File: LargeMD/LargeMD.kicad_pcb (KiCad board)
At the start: 2 copper layers, 110 x 60 mm, 189 parts, among them J1 Conn_01x02_Male, J10 Conn_01x04_Male, J2 Conn_01x02_Female, J3 Conn_01x10_Male, J4 Conn_01x02_Male, J5 Conn_01x03_Male, J6 Conn_01x02_Female, J7 Conn_01x04_Male, J8 Conn_01x04_Male, J9 Conn_01x04_Male, Q1 TJ60S04M3L, Q10 S8050, Q11 SSM3J332R, Q12 S8050, Q13 SSM3J332R, Q14 S8050, Q15 S8050, Q16 S8050, Q17 BSS138, Q18 BSS138, Q19 TPH3R704PL, Q2 BSS138, Q20 TPH3R704PL, Q21 TPH3R704PL, Q22 TPH3R704PL, Q3 TJ60S04M3L, Q4 S8050, Q5 SSM3J332R, Q6 S8050, Q7 SSM3J332R, Q8 S8050, Q9 SSM3J332R, SW1 SW_DIP_x05, SW2 SW_SPDT, SW3 SW_SPDT, SW4 SW_SPST, U1 LF50_TO220, U10 IR2302, U2 AZ1084CD-3.3, U3 STM32C031K4T6, U4 LT6106, U5 MAX3485, U6 MAX3485, U7 TLP2361, U8 TLP2361, U9 IR2302, Y1 48MHz

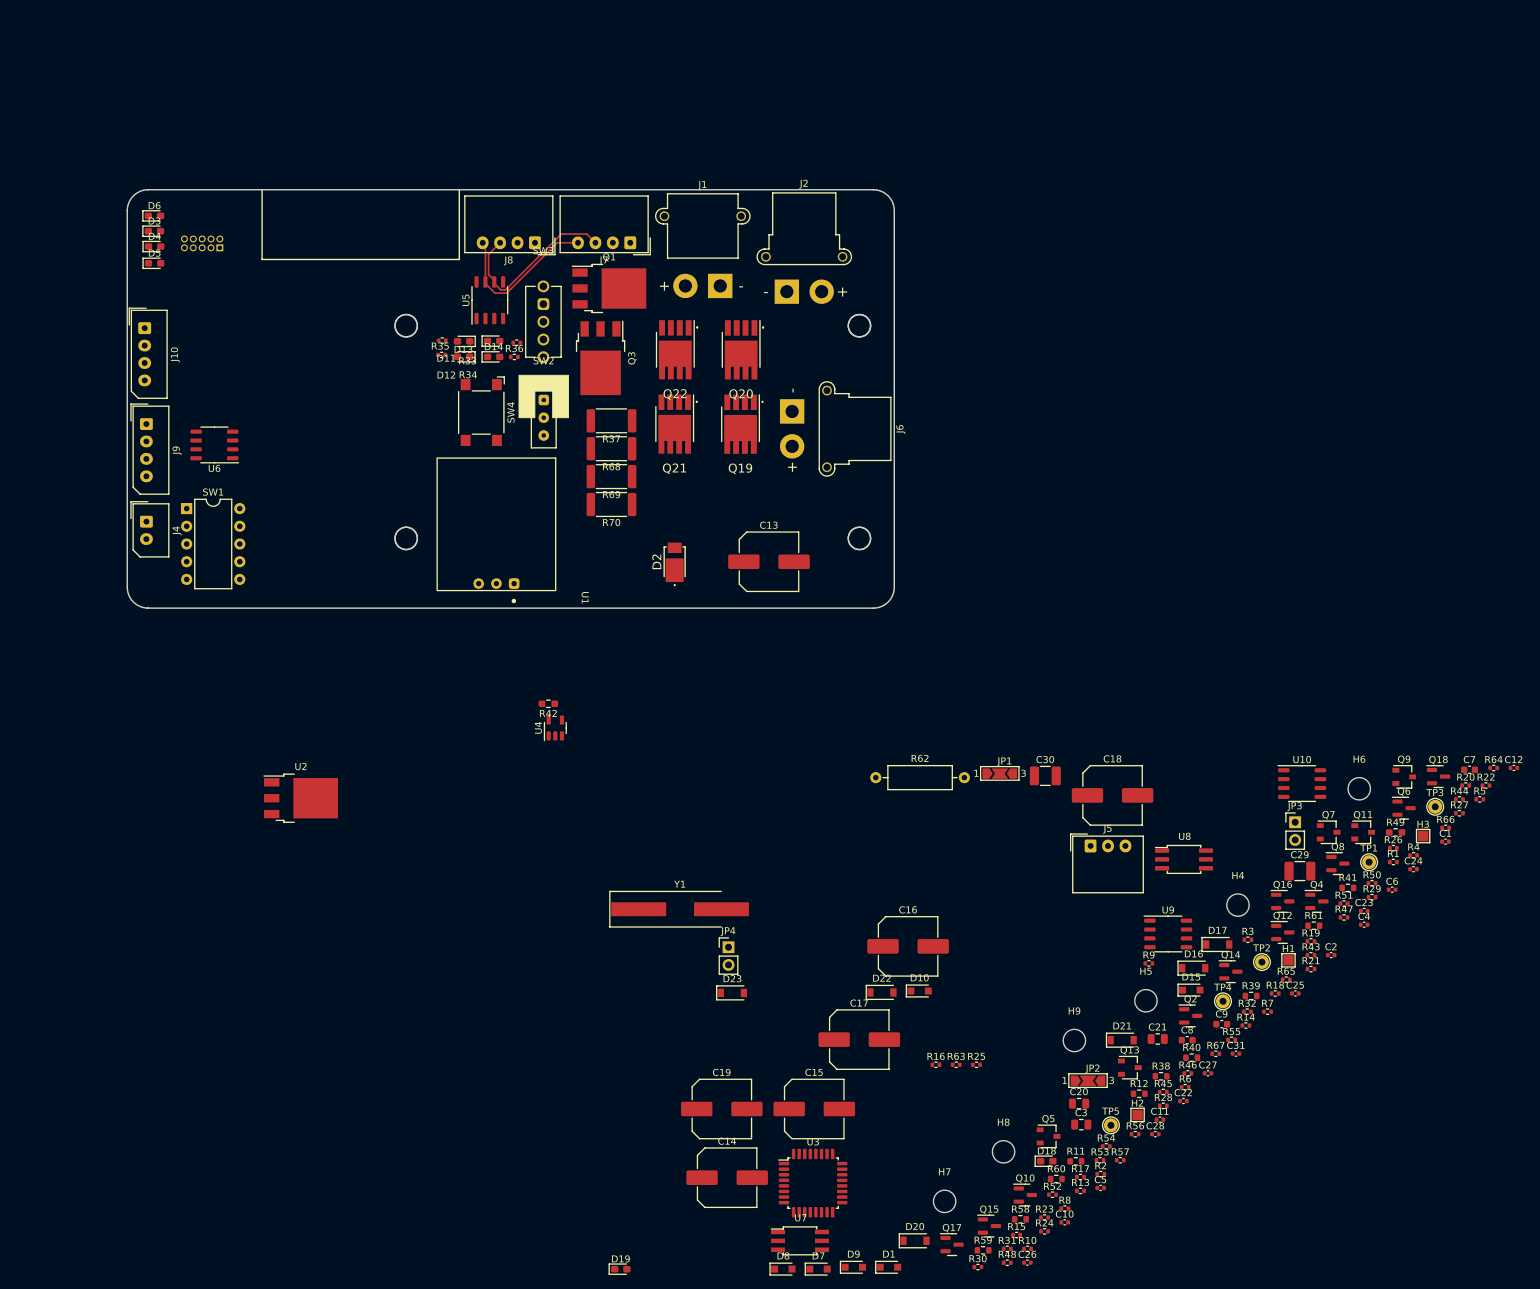
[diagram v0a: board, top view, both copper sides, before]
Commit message: エンコーダー基板配線完了
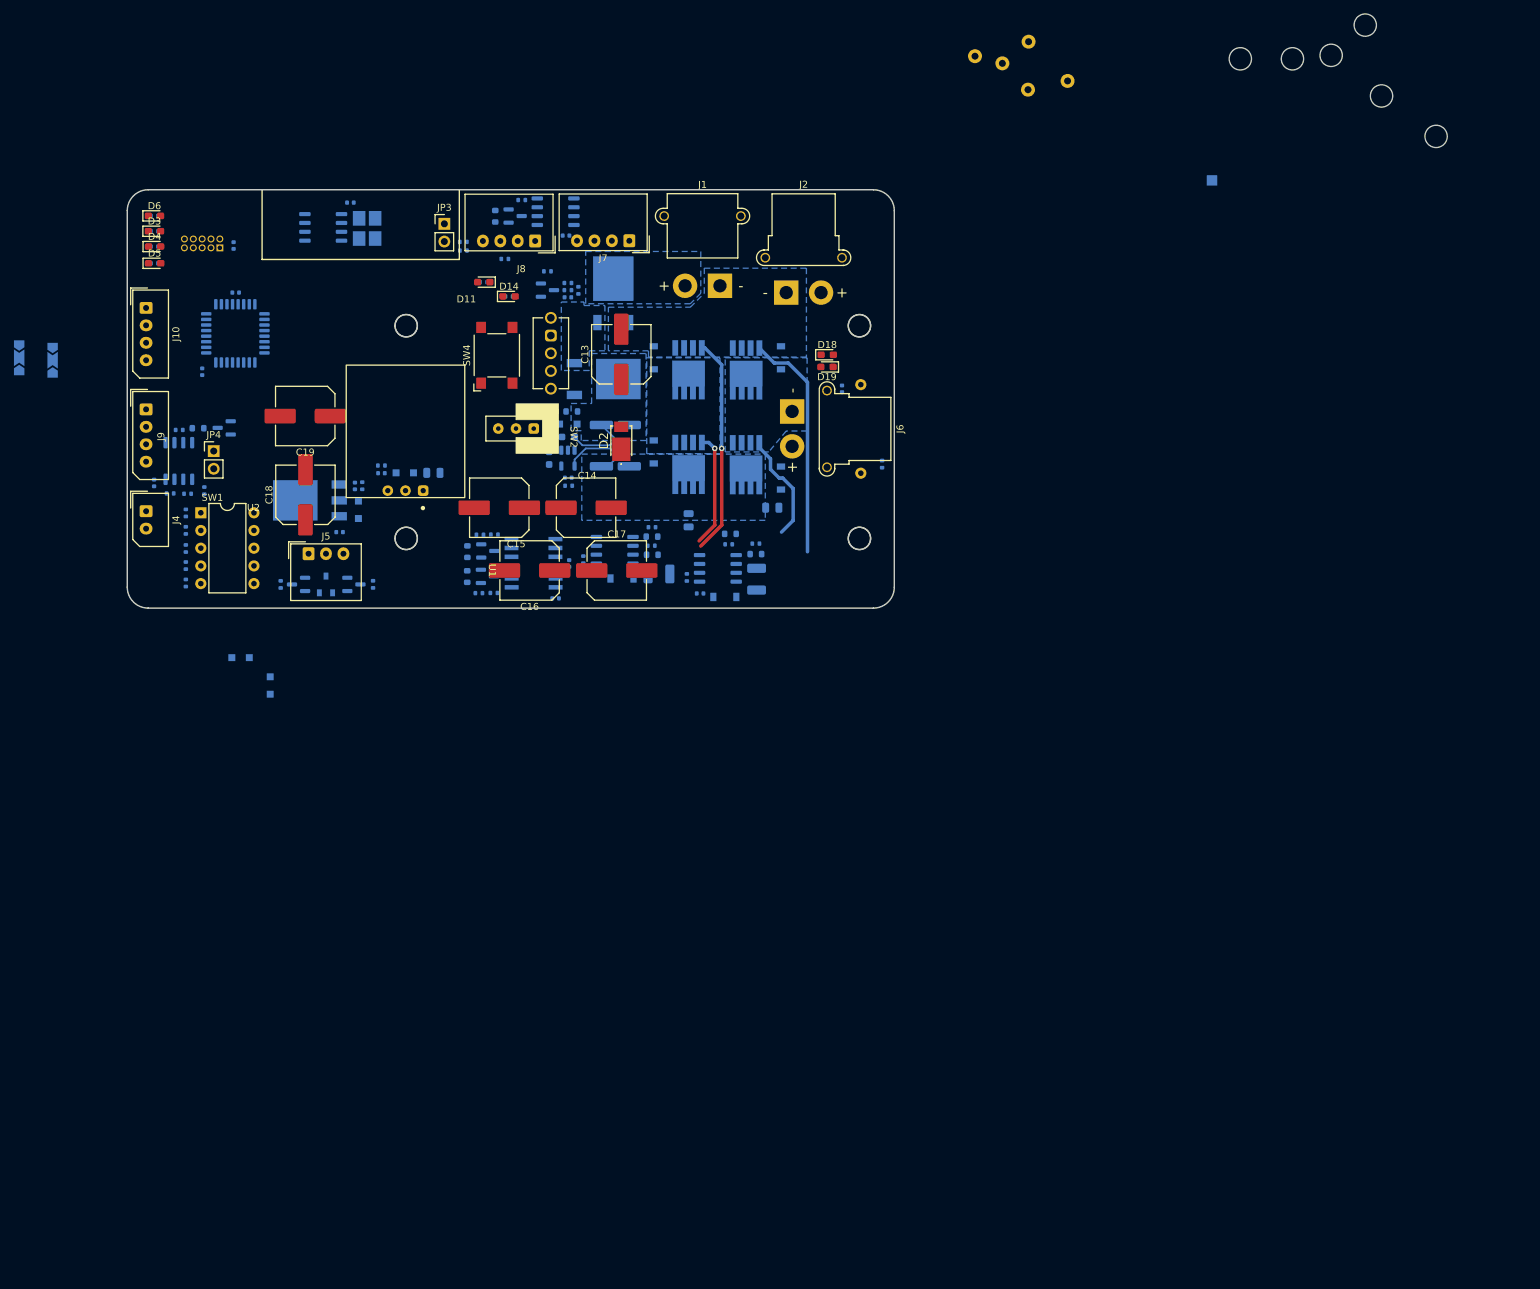
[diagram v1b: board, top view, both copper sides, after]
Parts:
- removed C12: 1uF, Capacitor_SMD:C_0402_1005Metric
- removed C8, C9: 22pF, Capacitor_SMD:C_0603_1608Metric
- removed D10: D_Zener, Diode_SMD:D_SOD-323_HandSoldering
- removed D12, D13: Green, LED_SMD:LED_0603_1608Metric_Pad1.05x0.95mm_HandSolder
- removed H1, H3: MountingHole_Pad, TestPoint:TestPoint_Pad_1.5x1.5mm
- removed Q10, Q12, Q14, Q8: S8050, Package_TO_SOT_SMD:SOT-23
- removed Q11, Q13, Q7, Q9: SSM3J332R, Package_TO_SOT_SMD:SOT-23W
- removed R21, R23, R25, R26, R28, R29, R30, R31, R32: 10k, Resistor_SMD:R_0402_1005Metric
- removed R24, R34, R35: 1k, Resistor_SMD:R_0402_1005Metric
- removed R27: 100k, Resistor_SMD:R_0402_1005Metric
- removed R69, R70: 40mR, Resistor_SMD:R_2512_6332Metric
- added U11: NJU6319AE, Package_SO:SOP-8_3.9x4.9mm_P1.27mm, B.Cu at (70.6, 40.5)
- C1, C10, C11, C2, C20, C21, C22, C23, C24, C25, C26, C27, C28, C29, C3, C30, C31, C4, C5, C6, D1, D15, D16, D17, D20, D21, D22, D23, D7, D8, D9, H2, H4, H5, H6, H7, H8, H9, JP1, JP2, Q15, Q16, Q17, Q18, Q19, Q2, Q20, Q21, Q22, Q4, Q5, Q6, R1, R10, R11, R12, R13, R14, R15, R16, R17, R18, R19, R2, R20, R22, R3, R33, R36, R38, R39, R4, R40, R41, R42, R43, R44, R45, R46, R47, R48, R49, R5, R50, R51, R52, R53, R54, R55, R56, R57, R58, R59, R6, R60, R61, R62, R63, R64, R65, R66, R67, R7, R8, R9, TP1, TP2, TP3, TP4, TP5, U10, U2, U3, U4, U5, U6, U7, U8, U9: moved to B.Cu
- C7: value ADJ_ST -> 0.1uF; footprint Capacitor_SMD:C_0603_1608Metric -> Capacitor_SMD:C_0402_1005Metric; moved to B.Cu
- Q1, Q3: footprint Package_TO_SOT_SMD:TO-252-3_TabPin2 -> Package_TO_SOT_SMD:TO-252-2; moved to B.Cu
- R37, R68: value 40mR -> 20mR; moved to B.Cu
- Y1: value 48MHz -> 16MHz; footprint Crystal:Crystal_SMD_HC49-SD_HandSoldering -> Crystal:Crystal_SMD_3225-4Pin_3.2x2.5mm_HandSoldering; moved to B.Cu
- moved R14 192.3 mm to (46.4, 43.3), turned to 180 degrees
- moved R13 191.3 mm to (46.4, 41.1), turned to 180 degrees
- moved R5 188.6 mm to (50.9, 89.0), turned to 90 degrees
- moved C2 187.4 mm to (57.8, 43.1), turned to 90 degrees
- moved R15 186.3 mm to (46.4, 45.7), turned to 180 degrees
- moved JP2 185.1 mm to (27.0, 59.2), turned to -90 degrees
- moved R1 180.3 mm to (50.9, 81.5), turned to 90 degrees
- moved C7 179.9 mm to (74.5, 37.0)
- moved C11 177.9 mm to (58.0, 49.9)
- moved R41 177.6 mm to (52.6, 69.3), turned to 180 degrees
- moved C10 173.7 mm to (53.2, 61.2), turned to -90 degrees
- moved R46 171.6 mm to (50.0, 69.6)
- moved H7 170.5 mm to (222.4, 21.7), turned to 180 degrees
- moved C26 167.9 mm to (46.4, 77.2), turned to -90 degrees
- moved R22 166.8 mm to (76.2, 77.6), turned to -90 degrees
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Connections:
- C31 pad 2: Motor_B -> Motor_A
- C6 pad 1: /3.3VSYS -> +3.3V
- C7 pad 1: GND -> +3.3V
- C7 pad 2: Net-(C7-Pad2) -> GND
- D18 pad 1: Motor_B -> Motor_A
- D19 pad 2: Motor_B -> Motor_A
- D8 pad 2: /3.3VSYS -> +3.3V
- R22 pad 2: /3.3VSYS -> +3.3V
- R62 pad 1: Motor_A -> Motor_B
- R67 pad 2: Motor_A -> Motor_B
- U2 pad 2: /3.3VSYS -> +3.3V
- U3 pad 2: unconnected-(U3-Pad2) -> OSC_IN
- U3 pad 6: unconnected-(U3-Pad6) -> NRST
- Y1 pad 1: OSC_OUT -> Net-(U11-Pad2)
- Y1 pad 2: OSC_IN -> GND
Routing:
- net Net-(Q20-Pad4): track 0.00 -> 33.2 mm
- net Net-(Q22-Pad4): track 0.00 -> 31.1 mm, vias 0 -> 1
- net RS485a_A: track 25.6 -> 0.00 mm
- net RS485a_B: track 22.8 -> 0.52 mm
- net Net-(Q21-Pad4): track 0.00 -> 16.4 mm, vias 0 -> 1
- net Net-(Q19-Pad4): track 0.00 -> 15.8 mm
- net Vdrive: track 0.00 -> 10.7 mm
- net VDD: track 0.00 -> 9.46 mm
- added copper zone on B.Cu, net /12VBAT
- added copper zone on B.Cu, net /S-S
- added copper zone on B.Cu, net GND
- added copper zone on B.Cu, net Motor_A
- added copper zone on B.Cu, net Motor_B
- added copper zone on B.Cu, net VDD
- added copper zone on B.Cu, net Vdrive

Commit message: LargeMD
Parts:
- removed C2: 0.1uF, Capacitor_SMD:C_0402_1005Metric
- moved TP1 44.8 mm to (158.8, 60.9)
- moved JP2 28.2 mm to (54.6, 53.5), turned to 90 degrees
- moved JP1 20.7 mm to (51.5, 53.5)
- moved R50 13.1 mm to (108.9, 40.6), turned to 0 degrees
- moved C10 11.3 mm to (64.3, 58.7)
- moved U3 11.3 mm to (69.0, 53.2)
- moved C11 11.3 mm to (69.0, 47.4)
- moved R9 11.0 mm to (97.6, 56.0), turned to 90 degrees
- moved D2 10.8 mm to (102.7, 72.8), turned to 0 degrees
- moved C1 8.88 mm to (98.6, 56.0), turned to -90 degrees
- moved R8 8.80 mm to (99.7, 56.0), turned to -90 degrees
- moved R7 7.68 mm to (100.9, 54.0)
- moved R4 7.52 mm to (99.4, 62.5), turned to 180 degrees
- moved R10 5.49 mm to (100.9, 52.0), turned to -90 degrees
- moved Q2 5.43 mm to (98.6, 53.0), turned to -90 degrees
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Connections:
- J3 pad 1: /3.3VBUS -> unconnected-(J3-Pad1)
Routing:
- net +5V: track 0.00 -> 102.2 mm
- net +3.3V: track 0.00 -> 64.7 mm, vias 0 -> 3
- net Motor_A: track 0.00 -> 54.4 mm, vias 0 -> 60
- net Motor_B: track 0.00 -> 47.3 mm, vias 0 -> 113
- net Net-(J4-Pad2): track 0.00 -> 39.9 mm
- net VCC: track 0.00 -> 35.8 mm
- net RS485b_A: track 0.00 -> 32.2 mm
- net RS485a_A: track 0.00 -> 31.1 mm
- net RS485b_B: track 0.00 -> 28.2 mm
- net RS485a_B: track 0.52 -> 26.2 mm
- net Net-(R54-Pad2): track 0.00 -> 24.0 mm
- net SHDN: track 0.00 -> 20.9 mm
- net Net-(D18-Pad2): track 0.00 -> 18.3 mm, vias 0 -> 1
- net Net-(C1-Pad2): track 0.00 -> 13.0 mm
- net STLinkTX: track 0.00 -> 12.9 mm
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- added copper zone on F.Cu, net GND
- added copper zone on F.Cu, net Motor_A
- added copper zone on F.Cu, net Motor_B
- added copper zone on F.Cu, net VCC
- added copper zone on F.Cu, net VDD
- added copper zone on F.Cu, net Vdrive

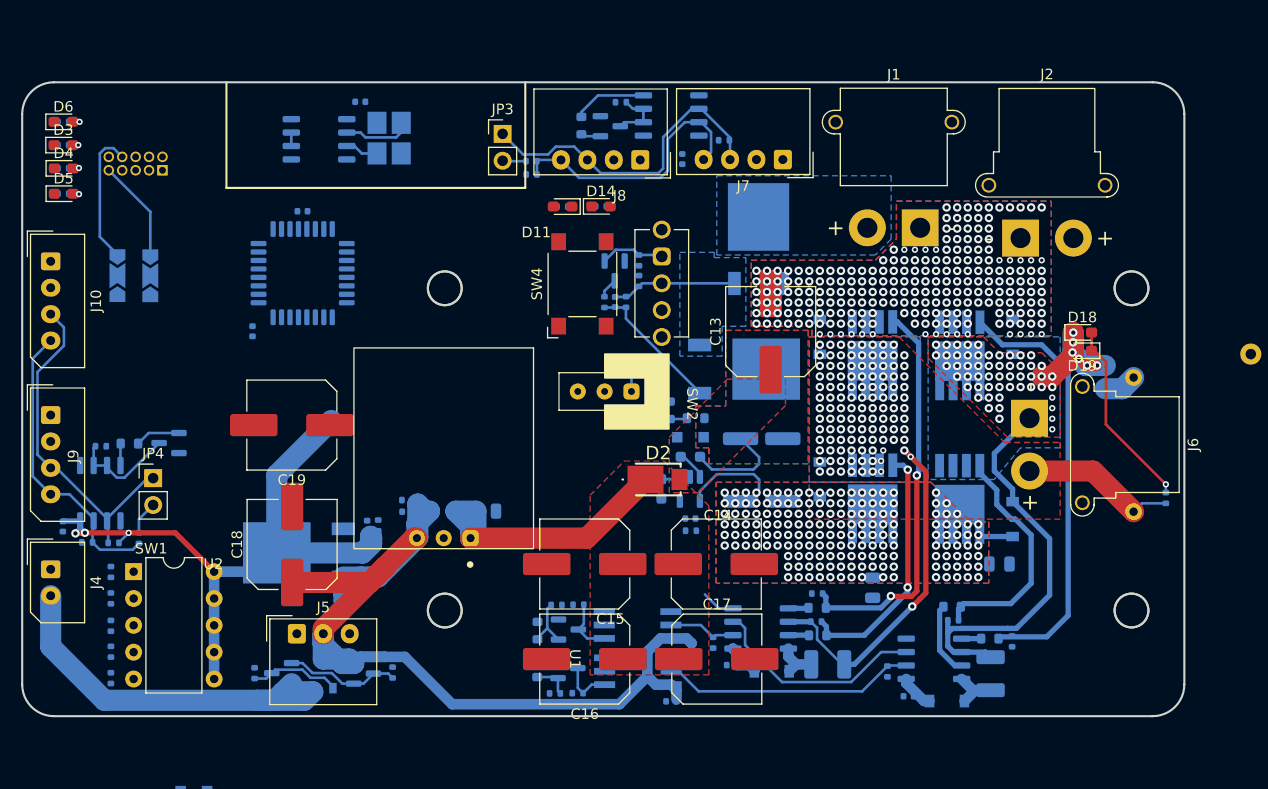
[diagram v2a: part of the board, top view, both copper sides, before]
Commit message: 人力曲面配線中
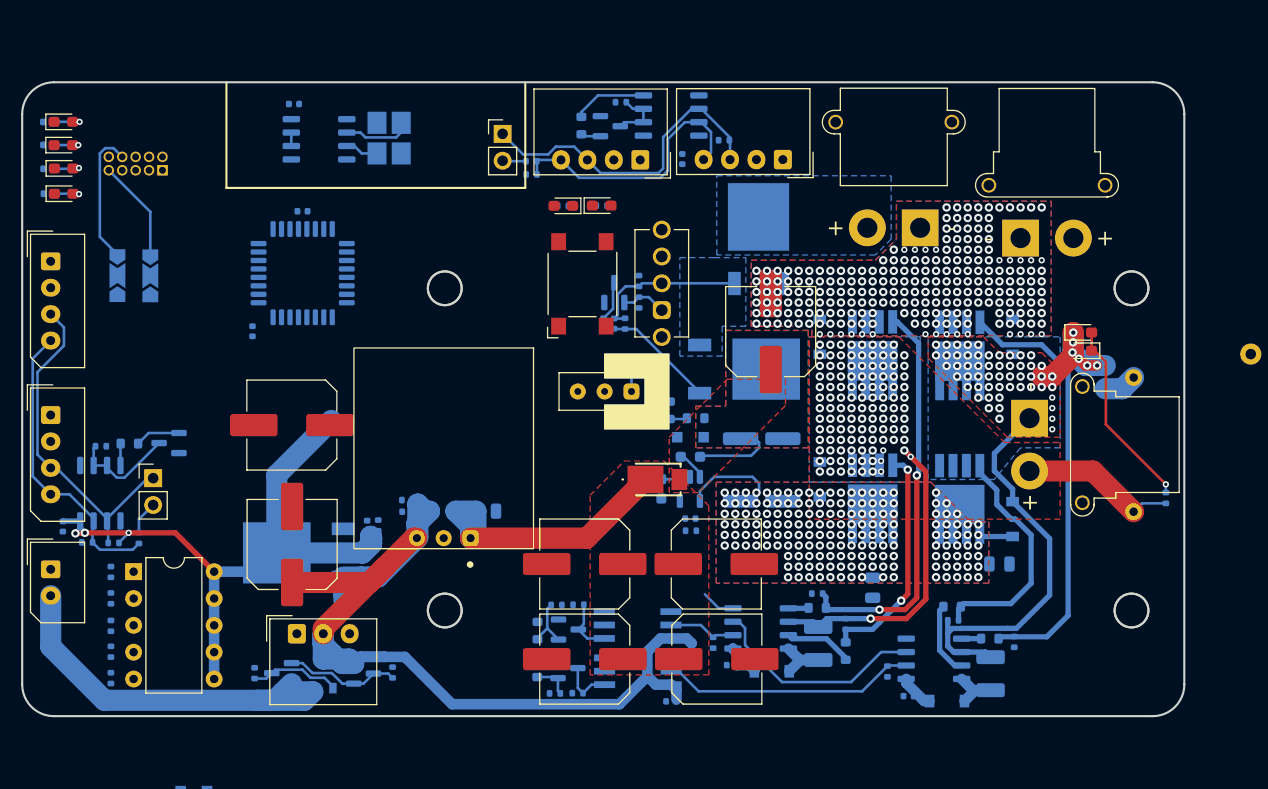
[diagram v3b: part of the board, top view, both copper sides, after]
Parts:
- moved C7 6.27 mm to (68.2, 37.2)
- moved R10 3.99 mm to (100.9, 56.0)
- moved R60 3.04 mm to (120.5, 89.0), turned to 90 degrees
- moved R65 2.80 mm to (120.4, 86.4), turned to -90 degrees
- moved C30 2.17 mm to (117.8, 88.3), turned to 90 degrees
- moved Q2 2.05 mm to (98.5, 55.1), turned to 90 degrees
- moved C1 2.05 mm to (98.5, 58.0)
- moved R8 2.05 mm to (99.6, 58.0)
- moved R9 2.04 mm to (97.5, 58.0)
- moved R16 1.43 mm to (45.0, 38.9)
- moved R13 1.42 mm to (45.0, 41.1)
- moved R14 1.41 mm to (45.0, 43.3)
- moved R15 1.38 mm to (45.0, 45.7)
- moved R64 0.21 mm to (136.4, 88.1)
- moved R33 0.10 mm to (93.7, 46.9)
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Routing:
- net Net-(R60-Pad1): track 1.96 -> 6.49 mm
- net Motor_B: track 47.3 -> 44.1 mm
- net /S-S: track 11.8 -> 15.0 mm
- net Net-(Q21-Pad4): track 24.1 -> 21.9 mm
- net Net-(Q2-Pad3): track 1.90 -> 3.79 mm
- net 主電源スイッチ: track 6.11 -> 4.26 mm
- net Net-(D6-Pad2): track 1.68 -> 3.11 mm
- net Net-(D3-Pad2): track 1.44 -> 2.86 mm
- net Net-(D4-Pad2): track 1.55 -> 2.98 mm
- net Net-(C1-Pad2): track 13.0 -> 11.7 mm
- net Net-(D5-Pad2): track 1.58 -> 2.96 mm
- net VDD: track 9.46 -> 8.34 mm
- net Net-(C30-Pad1): track 4.15 -> 4.75 mm

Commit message: LargeMDほぼ完成
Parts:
- removed H4, H5, H6, H7, H8, H9: MountingHole, MountingHole:MountingHole_3.2mm_M3
- removed TP1, TP2, TP3: TestPoint, TestPoint:TestPoint_THTPad_D2.0mm_Drill1.0mm
- H2: moved to F.Cu
- U3: value STM32C031K4T6 -> STM32G030K6T6
- moved TP4 112.9 mm to (76.6, 70.3)
- moved H2 110.4 mm to (89.1, 51.6), turned to 0 degrees
- moved D15 47.9 mm to (95.7, 71.2), turned to 45 degrees
- moved TP5 45.0 mm to (149.1, 59.8)
- moved D9 32.8 mm to (66.9, 70.5)
- moved C10 9.83 mm to (70.4, 51.0), turned to 45 degrees
- moved U11 5.61 mm to (71.4, 46.1)
- moved Y1 5.61 mm to (78.1, 46.0)
- moved C7 5.61 mm to (69.1, 42.8)
- moved U3 4.21 mm to (65.1, 54.7), turned to -135 degrees
- moved JP2 3.76 mm to (52.6, 56.6), turned to 0 degrees
- moved C19 2.95 mm to (68.3, 70.5), turned to 0 degrees
- moved C11 2.52 mm to (69.3, 49.9), turned to 45 degrees
- moved JP1 1.19 mm to (52.6, 52.9), turned to 0 degrees
- moved C18 1.06 mm to (68.3, 79.9), turned to 180 degrees
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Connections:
- net RS485bRX renamed RS485aRX
- net RS485bTX renamed RS485aTX
- J10 pad 3: RS485b_A -> RS485a_A
- J10 pad 4: RS485b_B -> RS485a_B
- J7 pad 3: RS485a_A -> RS485b_A
- J7 pad 4: RS485a_B -> RS485b_B
- J8 pad 3: RS485a_A -> RS485b_A
- J8 pad 4: RS485a_B -> RS485b_B
- J9 pad 3: RS485b_A -> RS485a_A
- J9 pad 4: RS485b_B -> RS485a_B
- JP1 pad 2: MainRX_RS485bTX -> MainRX1_RS485aTX
- JP2 pad 2: MainTX_RS485bRX -> MainTX1_RS485aRX
- JP3 pad 1: RS485a_A -> RS485b_A
- JP4 pad 1: RS485b_A -> RS485a_A
- R40 pad 2: MainTX_RS485aRX -> MainTX2_RS485bRX
- R50 pad 2: RS485a_A -> RS485b_A
- R51 pad 1: RS485a_B -> RS485b_B
- R52 pad 2: RS485b_A -> RS485a_A
- R53 pad 1: RS485b_B -> RS485a_B
- R56 pad 2: RS485a_B -> RS485b_B
- R57 pad 2: RS485b_B -> RS485a_B
- U11 pad 6: Net-(U11-Pad6) -> unconnected-(U11-Pad6)
- U11 pad 7: Net-(U11-Pad6) -> unconnected-(U11-Pad7)
- U3 pad 10: unconnected-(U3-Pad10) -> V_Measure
- U3 pad 11: unconnected-(U3-Pad11) -> Current_Sence
- U3 pad 12: unconnected-(U3-Pad12) -> SHDN
- U3 pad 13: unconnected-(U3-Pad13) -> PWM_A
- U3 pad 15: unconnected-(U3-Pad15) -> Sensor0
- U3 pad 16: unconnected-(U3-Pad16) -> DIP_SW4
- U3 pad 17: unconnected-(U3-Pad17) -> DIP_SW3
- U3 pad 18: unconnected-(U3-Pad18) -> DIP_SW2
- U3 pad 19: unconnected-(U3-Pad19) -> MainTX1_RS485aRX
- U3 pad 20: unconnected-(U3-Pad20) -> DIP_SW1
- U3 pad 21: unconnected-(U3-Pad21) -> MainRX1_RS485aTX
- U3 pad 22: unconnected-(U3-Pad22) -> DIP_SW0
- U3 pad 24: unconnected-(U3-Pad24) -> TMS
- U3 pad 25: unconnected-(U3-Pad25) -> TCK
- U3 pad 26: unconnected-(U3-Pad26) -> MainRX2_RS485bTX
- U3 pad 27: unconnected-(U3-Pad27) -> LED2
- U3 pad 28: unconnected-(U3-Pad28) -> LED1
- U3 pad 29: unconnected-(U3-Pad29) -> LED0
- U3 pad 30: unconnected-(U3-Pad30) -> PWM_B
- U3 pad 31: unconnected-(U3-Pad31) -> MonitorLED0
- U3 pad 8: unconnected-(U3-Pad8) -> Slide_SW0
- U3 pad 9: unconnected-(U3-Pad9) -> MainTX2_RS485bRX
- U5 pad 1: MainRX_RS485aTX -> MainRX2_RS485bTX
- U5 pad 4: MainTX_RS485aRX -> MainTX2_RS485bRX
- U5 pad 6: RS485a_A -> RS485b_A
- U5 pad 7: RS485a_B -> RS485b_B
- U6 pad 6: RS485b_A -> RS485a_A
- U6 pad 7: RS485b_B -> RS485a_B
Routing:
- net GND: track 3.20 -> 267.0 mm, vias 225 -> 679
- net +3.3V: track 64.7 -> 246.8 mm, vias 3 -> 13
- net NRST: track 0.00 -> 61.8 mm, vias 0 -> 2
- net SHDN: track 20.9 -> 75.1 mm
- net PWM_B: track 0.00 -> 52.5 mm, vias 0 -> 2
- net MainRX2_RS485bTX: track 0.00 -> 50.6 mm
- net PWM_A: track 0.00 -> 46.8 mm
- net MainTX2_RS485bRX: track 0.00 -> 43.8 mm, vias 0 -> 2
- net Current_Sence: track 1.84 -> 44.5 mm
- net DIP_SW4: track 0.00 -> 39.8 mm
- net VCC: track 35.8 -> 75.3 mm, vias 0 -> 3
- net V_Measure: track 1.65 -> 40.5 mm
- net DIP_SW3: track 0.00 -> 36.5 mm
- net Slide_SW0: track 2.01 -> 37.8 mm, vias 0 -> 2
- net DIP_SW2: track 0.00 -> 34.5 mm
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- added copper zone on F.Cu, net /S-S
